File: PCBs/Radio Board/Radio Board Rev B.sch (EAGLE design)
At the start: 4 parts

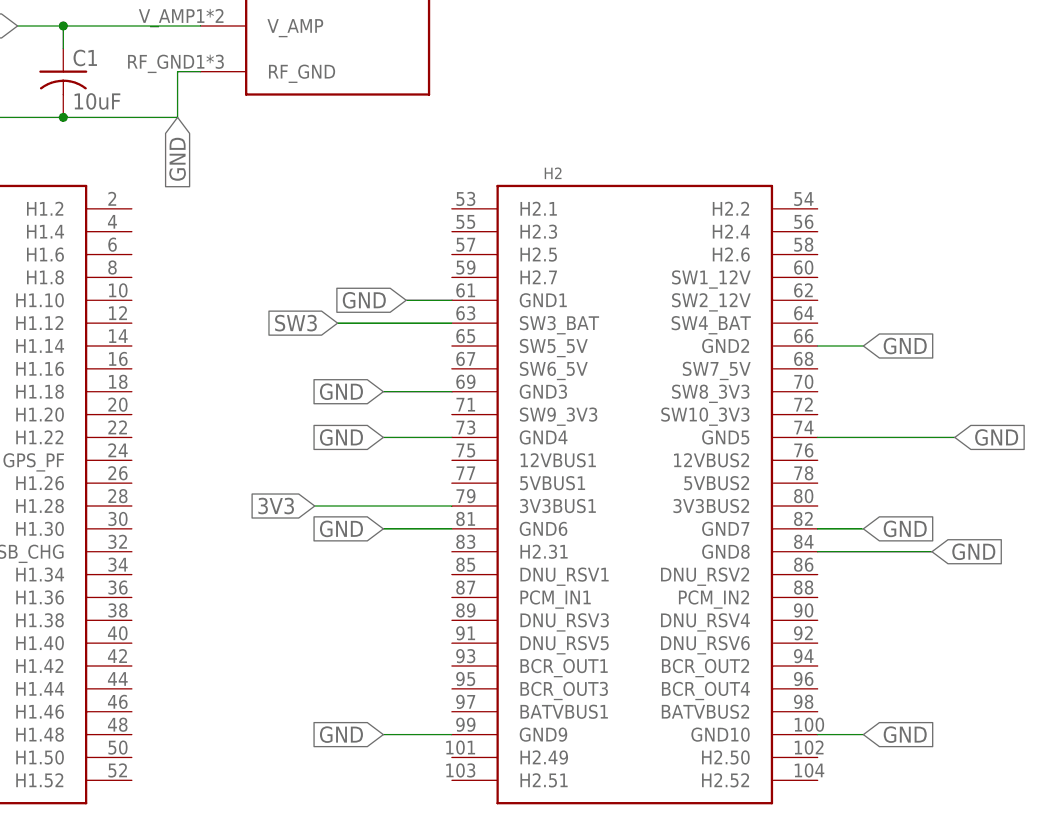
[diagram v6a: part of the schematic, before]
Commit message: Use different PC104 footprints for each board
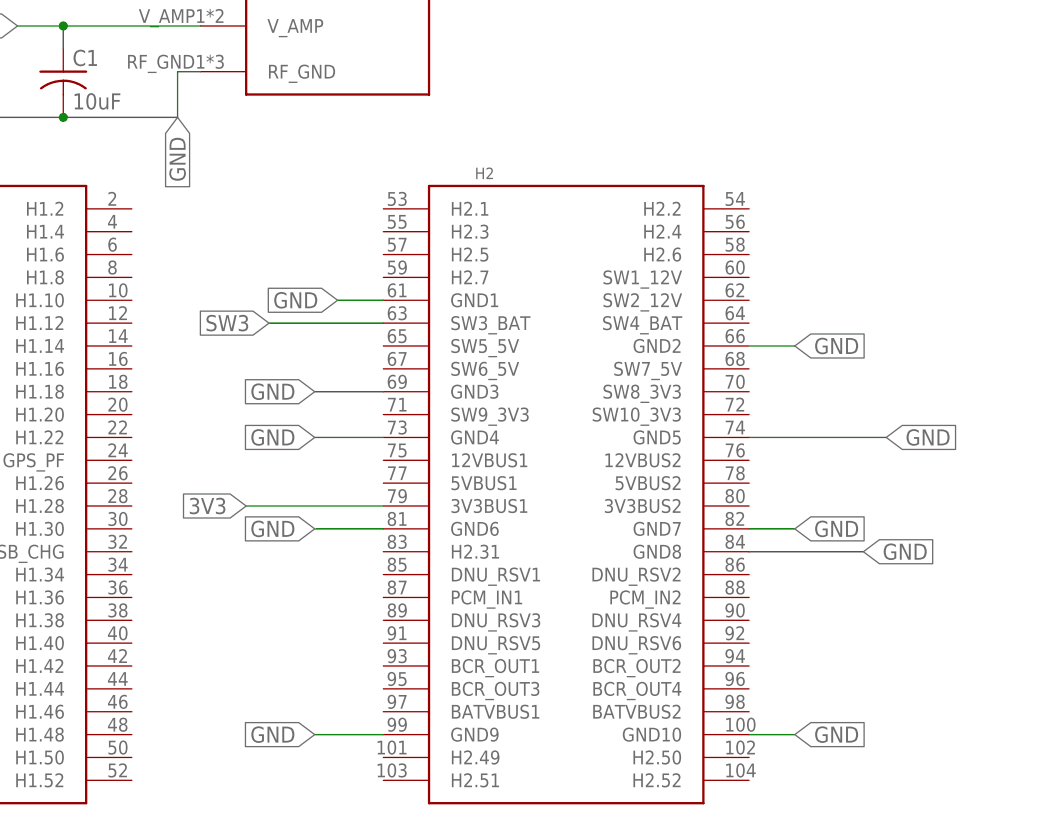
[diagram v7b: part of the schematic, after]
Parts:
- U$2: value PC104_BOARD -> PC104_RADIO; device Cubesat:PC104_BOARD -> Cubesat:PC104_RADIO
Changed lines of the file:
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@@
 <part name="C2" library="resistor" library_urn="urn:adsk.eagle:library:348" deviceset="C-US" device="C0805" package3d_urn="urn:adsk.eagle:package:26137/1" value="0.1uF"/>
 <part name="U$1" library="Cubesat" deviceset="LI-1" device=""/>
-<part name="U$2" library="Cubesat" deviceset="PC104_BOARD" device=""/>
+<part name="U$2" library="Cubesat" deviceset="PC104_RADIO" device=""/>
 </parts>
 <sheets>
@@
 <net name="GND" class="0">
 <segment>
-<wire x1="99.06" y1="55.88" x2="93.98" y2="55.88" width="0.1524" layer="91"/>
-<label x="93.98" y="55.88" size="1.778" layer="95" rot="R180" xref="yes"/>
+<wire x1="91.44" y1="55.88" x2="86.36" y2="55.88" width="0.1524" layer="91"/>
+<label x="86.36" y="55.88" size="1.778" layer="95" rot="R180" xref="yes"/>
 <pinref part="U$2" gate="A" pin="GND1"/>
 </segment>
 <segment>
-<wire x1="139.7" y1="40.64" x2="154.94" y2="40.64" width="0.1524" layer="91"/>
-<label x="154.94" y="40.64" size="1.778" layer="95" xref="yes"/>
+<wire x1="132.08" y1="40.64" x2="147.32" y2="40.64" width="0.1524" layer="91"/>
+<label x="147.32" y="40.64" size="1.778" layer="95" xref="yes"/>
 <pinref part="U$2" gate="A" pin="GND5"/>
 </segment>
@@
 </segment>
 <segment>
-<wire x1="99.06" y1="40.64" x2="91.44" y2="40.64" width="0.1524" layer="91"/>
-<label x="91.44" y="40.64" size="1.778" layer="95" rot="R180" xref="yes"/>
+<wire x1="91.44" y1="40.64" x2="83.82" y2="40.64" width="0.1524" layer="91"/>
+<label x="83.82" y="40.64" size="1.778" layer="95" rot="R180" xref="yes"/>
 <pinref part="U$2" gate="A" pin="GND4"/>
 </segment>
 <segment>
-<wire x1="139.7" y1="50.8" x2="144.78" y2="50.8" width="0.1524" layer="91"/>
-<label x="144.78" y="50.8" size="1.778" layer="95" xref="yes"/>
+<wire x1="132.08" y1="50.8" x2="137.16" y2="50.8" width="0.1524" layer="91"/>
+<label x="137.16" y="50.8" size="1.778" layer="95" xref="yes"/>
 <pinref part="U$2" gate="A" pin="GND2"/>
 </segment>
 <segment>
-<wire x1="99.06" y1="45.72" x2="91.44" y2="45.72" width="0.1524" layer="91"/>
-<label x="91.44" y="45.72" size="1.778" layer="95" rot="R180" xref="yes"/>
+<wire x1="91.44" y1="45.72" x2="83.82" y2="45.72" width="0.1524" layer="91"/>
+<label x="83.82" y="45.72" size="1.778" layer="95" rot="R180" xref="yes"/>
 <pinref part="U$2" gate="A" pin="GND3"/>
 </segment>
 <segment>
-<wire x1="99.06" y1="30.48" x2="91.44" y2="30.48" width="0.1524" layer="91"/>
-<label x="91.44" y="30.48" size="1.778" layer="95" rot="R180" xref="yes"/>
+<wire x1="91.44" y1="30.48" x2="83.82" y2="30.48" width="0.1524" layer="91"/>
+<label x="83.82" y="30.48" size="1.778" layer="95" rot="R180" xref="yes"/>
 <pinref part="U$2" gate="A" pin="GND6"/>
 </segment>
 <segment>
-<wire x1="99.06" y1="7.62" x2="91.44" y2="7.62" width="0.1524" layer="91"/>
-<label x="91.44" y="7.62" size="1.778" layer="95" rot="R180" xref="yes"/>
+<wire x1="91.44" y1="7.62" x2="83.82" y2="7.62" width="0.1524" layer="91"/>
+<label x="83.82" y="7.62" size="1.778" layer="95" rot="R180" xref="yes"/>
 <pinref part="U$2" gate="A" pin="GND9"/>
 </segment>
 <segment>
-<wire x1="139.7" y1="30.48" x2="144.78" y2="30.48" width="0.1524" layer="91"/>
-<label x="144.78" y="30.48" size="1.778" layer="95" xref="yes"/>
+<wire x1="132.08" y1="30.48" x2="137.16" y2="30.48" width="0.1524" layer="91"/>
+<label x="137.16" y="30.48" size="1.778" layer="95" xref="yes"/>
 <pinref part="U$2" gate="A" pin="GND7"/>
 </segment>
 <segment>
-<wire x1="139.7" y1="27.94" x2="152.4" y2="27.94" width="0.1524" layer="91"/>
-<label x="152.4" y="27.94" size="1.778" layer="95" xref="yes"/>
+<wire x1="132.08" y1="27.94" x2="144.78" y2="27.94" width="0.1524" layer="91"/>
+<label x="144.78" y="27.94" size="1.778" layer="95" xref="yes"/>
 <pinref part="U$2" gate="A" pin="GND8"/>
 </segment>
 <segment>
-<wire x1="139.7" y1="7.62" x2="144.78" y2="7.62" width="0.1524" layer="91"/>
-<label x="144.78" y="7.62" size="1.778" layer="95" xref="yes"/>
+<wire x1="132.08" y1="7.62" x2="137.16" y2="7.62" width="0.1524" layer="91"/>
+<label x="137.16" y="7.62" size="1.778" layer="95" xref="yes"/>
 <pinref part="U$2" gate="A" pin="GND10"/>
 </segment>
@@
 <net name="SW3" class="0">
 <segment>
-<wire x1="99.06" y1="53.34" x2="86.36" y2="53.34" width="0.1524" layer="91"/>
-<label x="86.36" y="53.34" size="1.778" layer="95" rot="R180" xref="yes"/>
+<wire x1="91.44" y1="53.34" x2="78.74" y2="53.34" width="0.1524" layer="91"/>
+<label x="78.74" y="53.34" size="1.778" layer="95" rot="R180" xref="yes"/>
 <pinref part="U$2" gate="A" pin="SW3_BAT"/>
 </segment>
@@
 <net name="3V3" class="0">
 <segment>
-<wire x1="99.06" y1="33.02" x2="83.82" y2="33.02" width="0.1524" layer="91"/>
-<label x="83.82" y="33.02" size="1.778" layer="95" rot="R180" xref="yes"/>
+<wire x1="91.44" y1="33.02" x2="76.2" y2="33.02" width="0.1524" layer="91"/>
+<label x="76.2" y="33.02" size="1.778" layer="95" rot="R180" xref="yes"/>
 <pinref part="U$2" gate="A" pin="3V3BUS1"/>
 </segment>

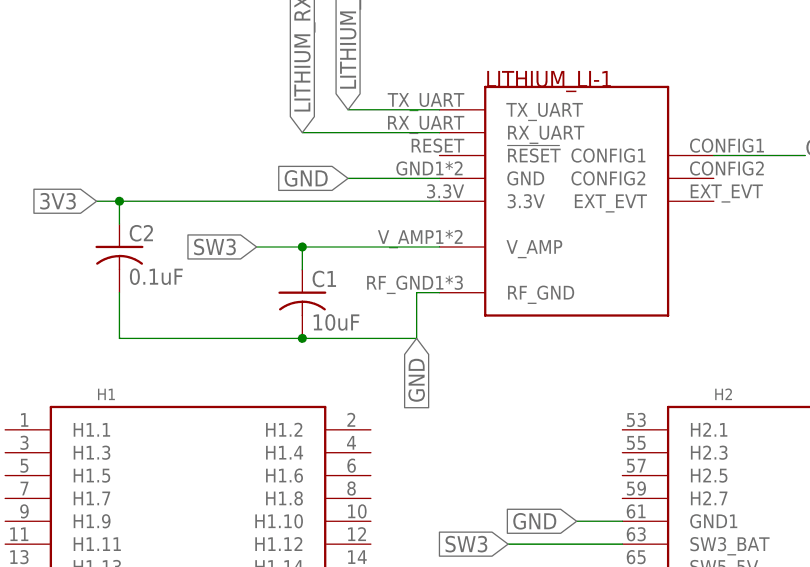
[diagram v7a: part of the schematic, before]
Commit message: Fix thermal/ground connection of radio
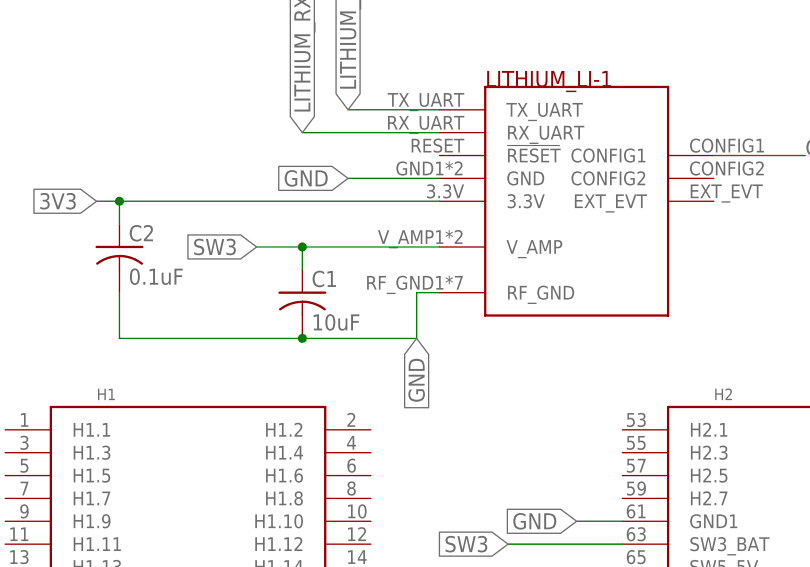
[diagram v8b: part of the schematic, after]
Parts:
- renumbered U$1 to LI-1
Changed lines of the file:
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@@
 <part name="C1" library="resistor" library_urn="urn:adsk.eagle:library:348" deviceset="C-US" device="C0805" package3d_urn="urn:adsk.eagle:package:26137/1" value="10uF"/>
 <part name="C2" library="resistor" library_urn="urn:adsk.eagle:library:348" deviceset="C-US" device="C0805" package3d_urn="urn:adsk.eagle:package:26137/1" value="0.1uF"/>
-<part name="U$1" library="Cubesat" deviceset="LI-1" device=""/>
+<part name="LI-1" library="Cubesat" deviceset="LI-1" device=""/>
 <part name="U$2" library="Cubesat" deviceset="PC104_RADIO" device=""/>
 </parts>
@@
 <instance part="C1" gate="G$1" x="55.88" y="81.28"/>
 <instance part="C2" gate="G$1" x="35.56" y="86.36"/>
-<instance part="U$1" gate="G$1" x="76.2" y="78.74"/>
+<instance part="LI-1" gate="G$1" x="76.2" y="78.74"/>
 <instance part="U$2" gate="A" x="22.86" y="66.04"/>
 </instances>
@@
 <wire x1="71.12" y1="93.98" x2="60.96" y2="93.98" width="0.1524" layer="91"/>
 <label x="60.96" y="93.98" size="1.778" layer="95" rot="R180" xref="yes"/>
-<pinref part="U$1" gate="G$1" pin="GND"/>
+<pinref part="LI-1" gate="G$1" pin="GND"/>
 </segment>
 <segment>
@@
 <wire x1="68.58" y1="81.28" x2="71.12" y2="81.28" width="0.1524" layer="91"/>
 <label x="68.58" y="76.2" size="1.778" layer="95" rot="R270" xref="yes"/>
-<pinref part="U$1" gate="G$1" pin="RF_GND"/>
+<pinref part="LI-1" gate="G$1" pin="RF_GND"/>
 </segment>
 </net>
@@
 <wire x1="55.88" y1="86.36" x2="55.88" y2="83.82" width="0.1524" layer="91"/>
 <junction x="55.88" y="86.36"/>
-<pinref part="U$1" gate="G$1" pin="V_AMP"/>
+<pinref part="LI-1" gate="G$1" pin="V_AMP"/>
 </segment>
 </net>
@@
 <wire x1="71.12" y1="101.6" x2="60.96" y2="101.6" width="0.1524" layer="91"/>
 <label x="60.96" y="101.6" size="1.778" layer="95" rot="R90" xref="yes"/>
-<pinref part="U$1" gate="G$1" pin="TX_UART"/>
+<pinref part="LI-1" gate="G$1" pin="TX_UART"/>
 </segment>
 <segment>
@@
 <wire x1="71.12" y1="99.06" x2="55.88" y2="99.06" width="0.1524" layer="91"/>
 <label x="55.88" y="99.06" size="1.778" layer="95" rot="R90" xref="yes"/>
-<pinref part="U$1" gate="G$1" pin="RX_UART"/>
+<pinref part="LI-1" gate="G$1" pin="RX_UART"/>
 </segment>
 <segment>
@@
 <junction x="35.56" y="91.44"/>
 <label x="33.02" y="91.44" size="1.778" layer="95" rot="R180" xref="yes"/>
-<pinref part="U$1" gate="G$1" pin="3.3V"/>
+<pinref part="LI-1" gate="G$1" pin="3.3V"/>
 </segment>
 </net>
@@
 <wire x1="101.6" y1="96.52" x2="111.76" y2="96.52" width="0.1524" layer="91"/>
 <label x="111.76" y="96.52" size="1.778" layer="95"/>
-<pinref part="U$1" gate="G$1" pin="CONFIG1"/>
+<pinref part="LI-1" gate="G$1" pin="CONFIG1"/>
 </segment>
 <segment>
